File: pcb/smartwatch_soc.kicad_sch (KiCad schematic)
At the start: 39 parts, among them J1 Battery Socket, J2 USB_A, Q1 PN2222A, Q2 PN2222A, Q3 PN2222A, SW1 EN_Switch, SW2 Button, SW3 Button, SW4 Button, SW5 Button, U1 ESP32-S3-MINI-1U, U2 LSM6DS3, U3 OLED_Display, U5 CP2102N-Axx-xQFN20

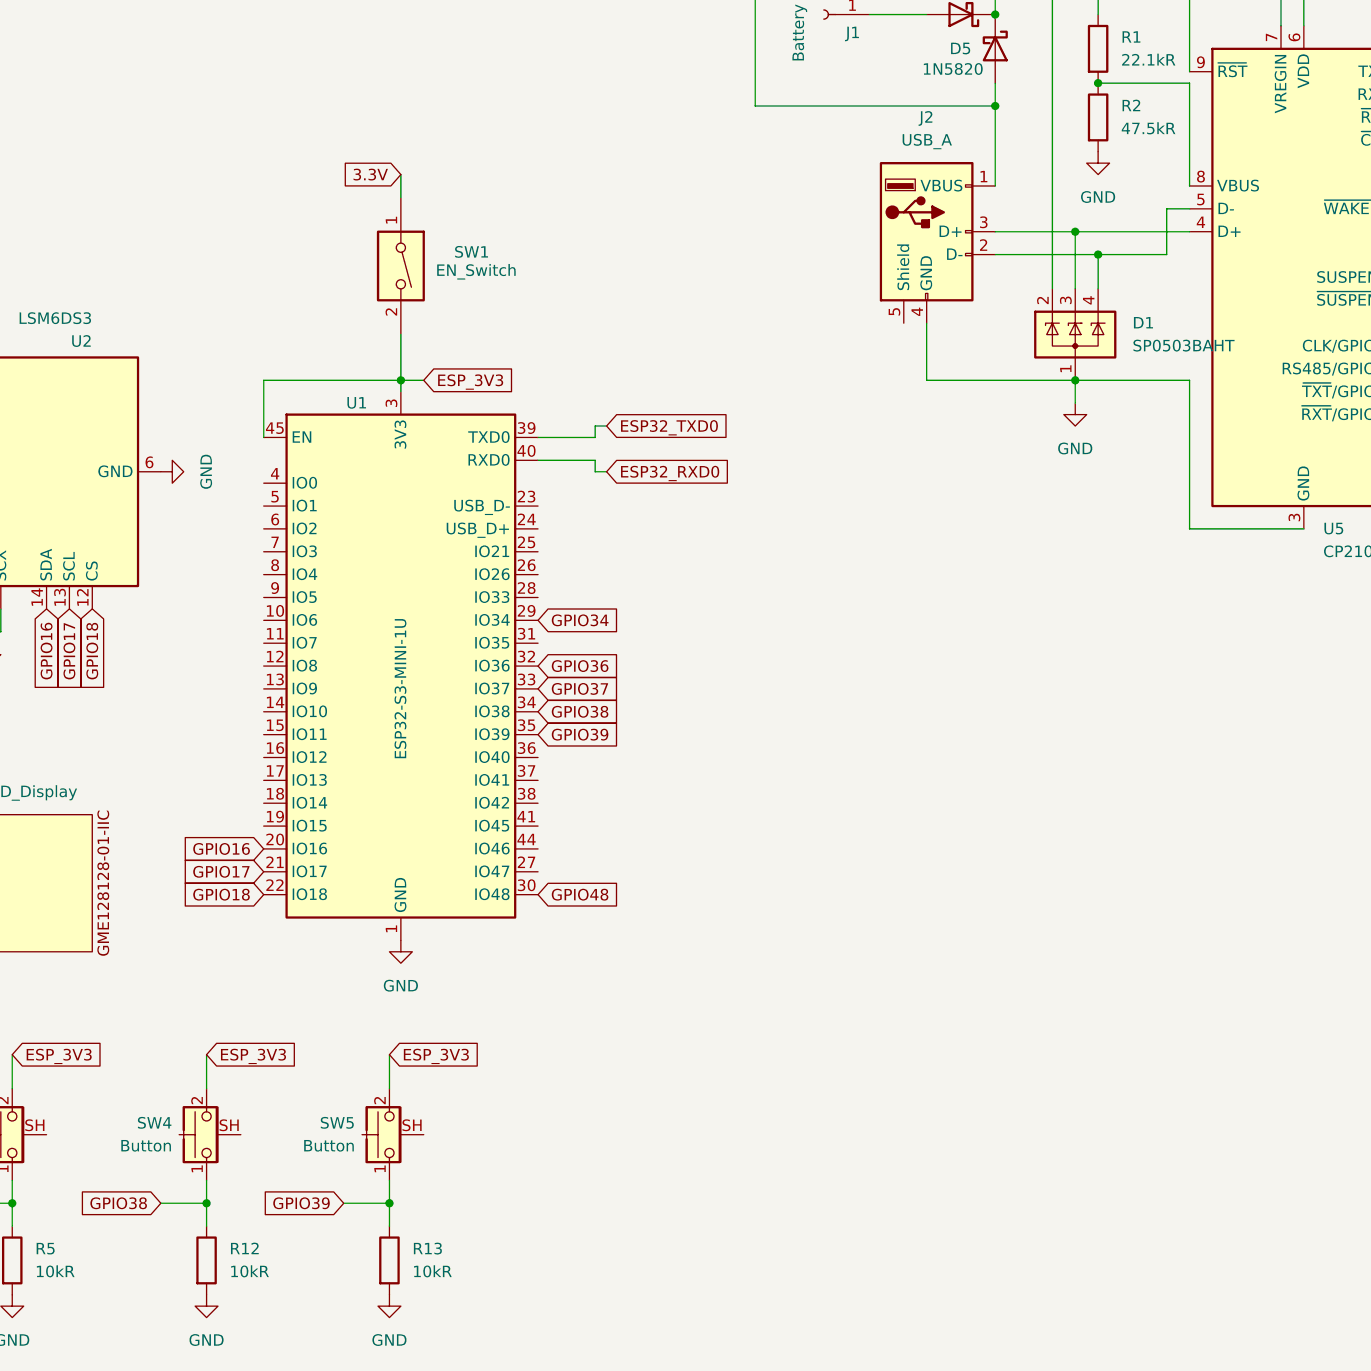
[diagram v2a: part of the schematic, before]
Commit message: added capacitors for en/3.3V for ESP32
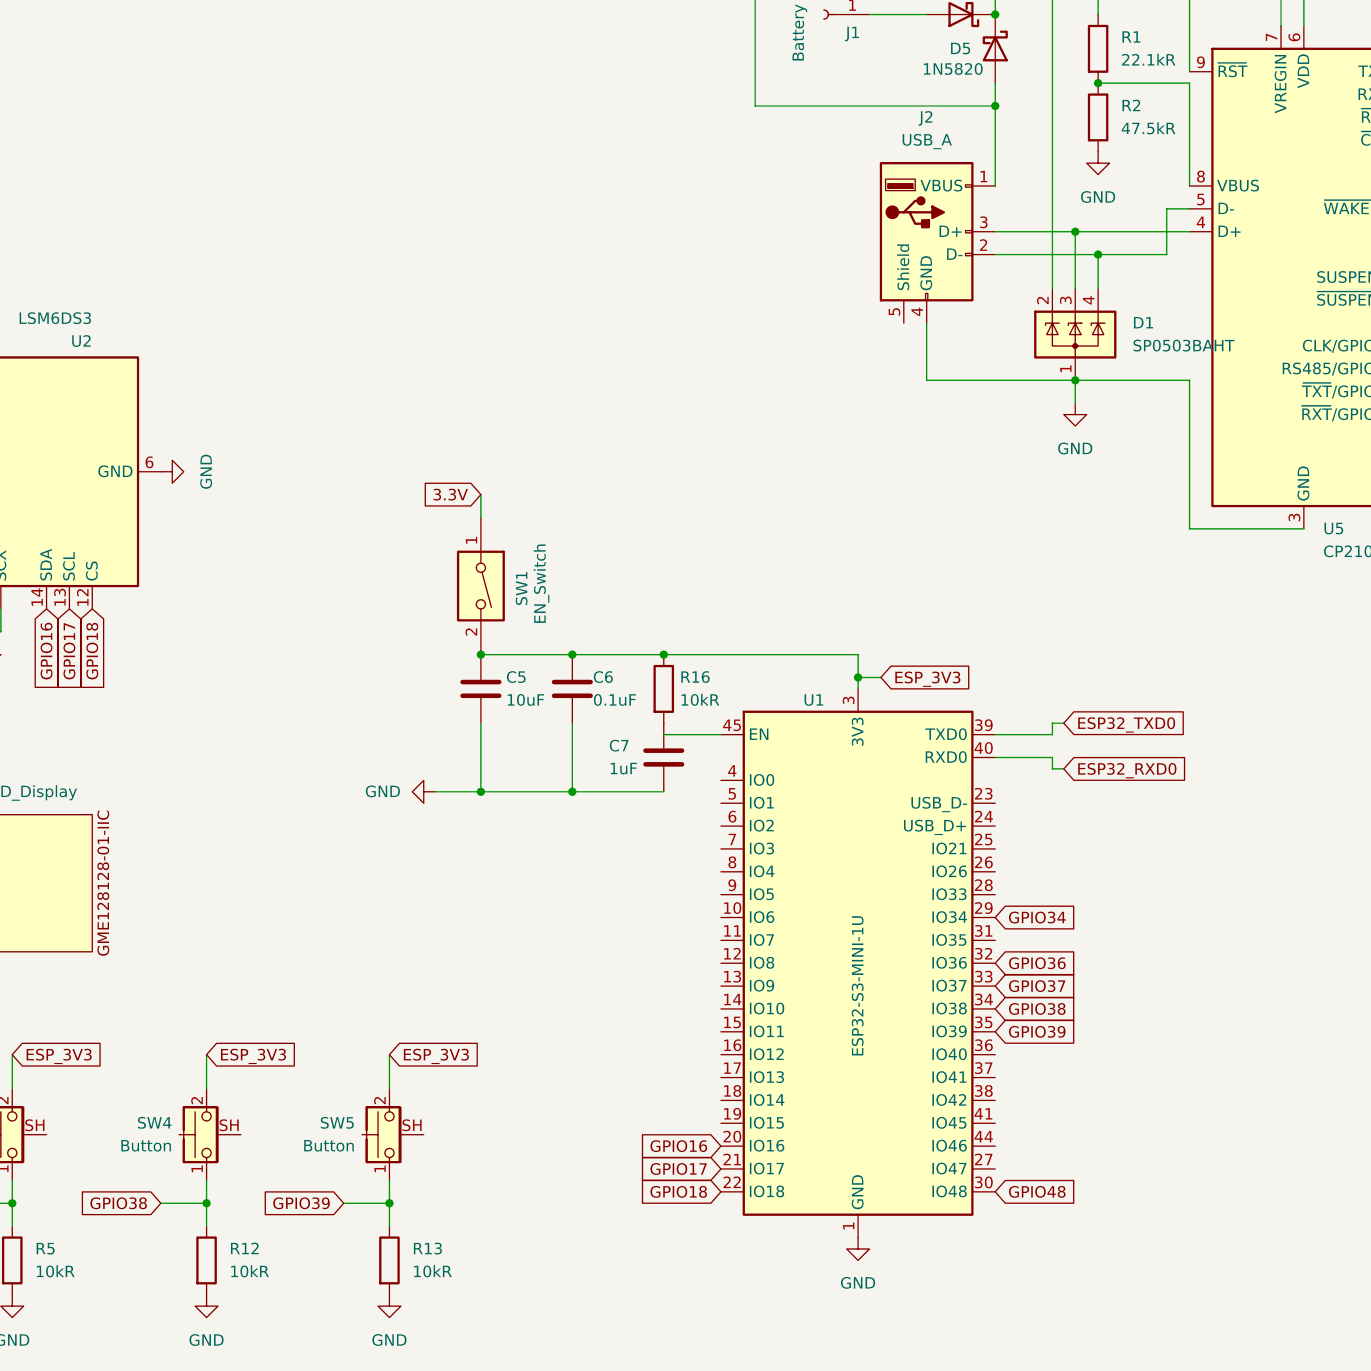
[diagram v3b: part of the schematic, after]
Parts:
- added C5: 10uF, symbol Device:C
- added C6: 0.1uF, symbol Device:C
- added C7: 1uF, symbol Device:C
- added R16: 10kR, symbol Device:R
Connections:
- net ESP_3V3: now also C5.1, C6.1, R16.1; no longer U1.45 (EN)
- net GND: now also C5.2, C6.2, C7.2
- new net: C7.1, R16.2
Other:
- moved on the sheet: SW1, U1

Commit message: bigger schematic page
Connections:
- net ESP32_GPIO0: now reaches U1.4 (IO0)
- net ESP_3V3 renamed ESP32_3V3
- net GPIO16 renamed ESP32_GPIO16
- net GPIO17 renamed ESP32_GPIO17
- net GPIO18 renamed ESP32_GPIO18
- net GPIO34 renamed ESP32_GPIO34
- net GPIO36 renamed ESP32_GPIO36
- net GPIO37 renamed ESP32_GPIO37
- net GPIO38 renamed ESP32_GPIO38
- net GPIO39 renamed ESP32_GPIO39
- net GPIO48 renamed ESP32_GPIO48
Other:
- moved on the sheet: C1, C2, C3, C4, C5, C6, C7, D1, D2, D3, D4, D5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

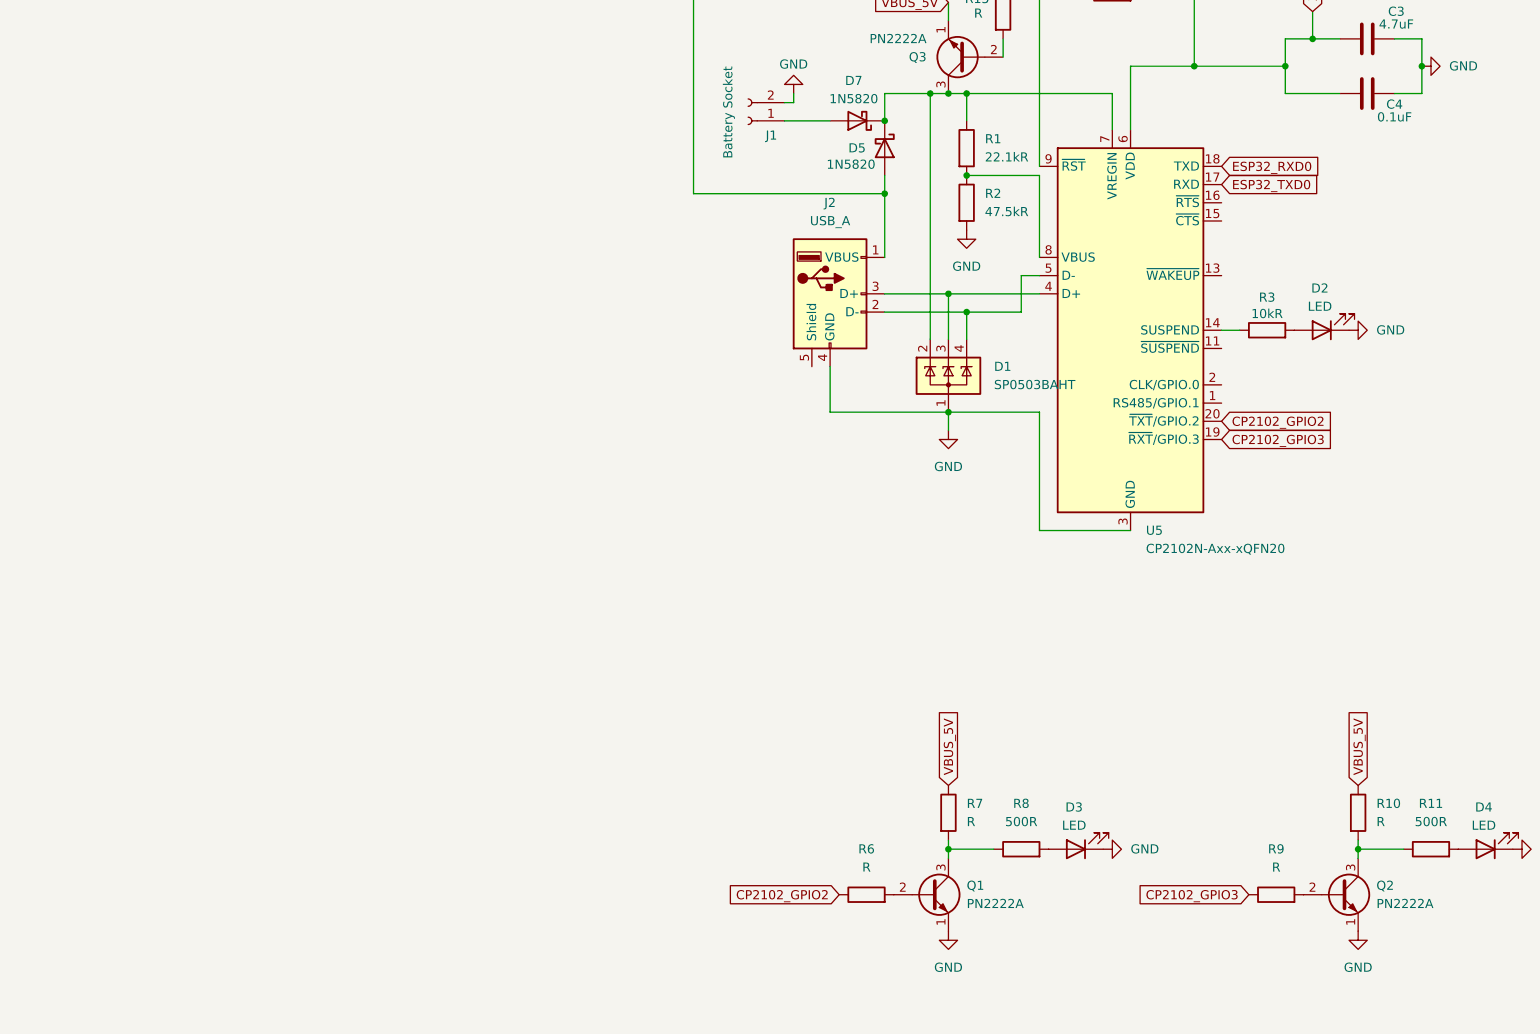
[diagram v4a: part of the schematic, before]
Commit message: switched usba to micro usb type b
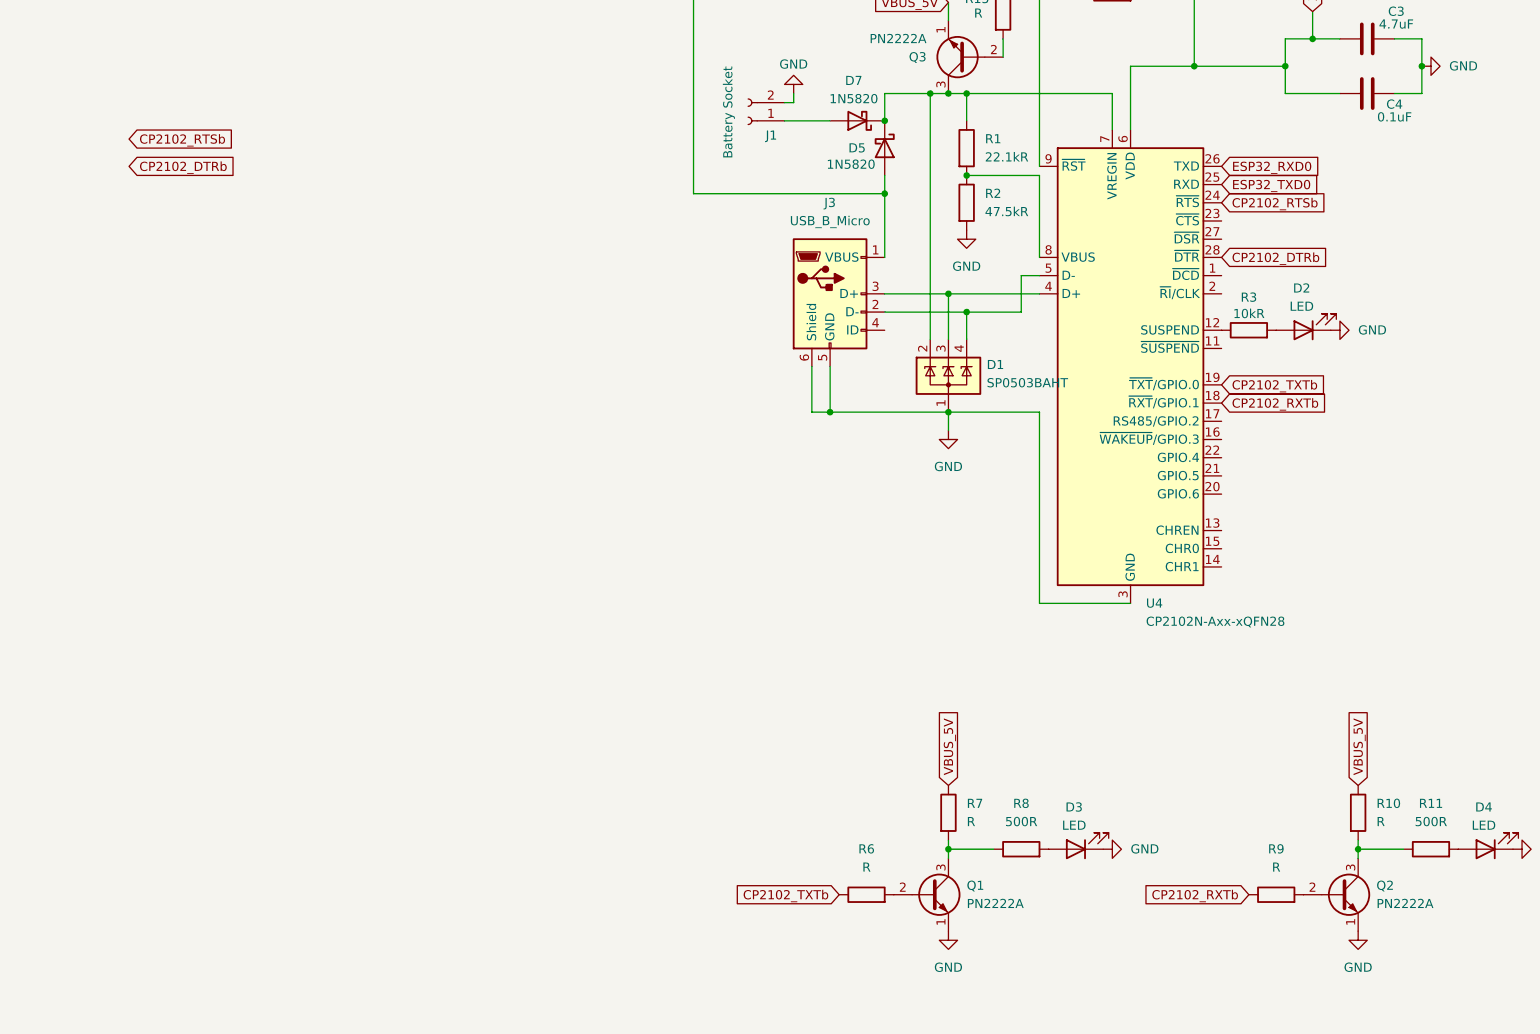
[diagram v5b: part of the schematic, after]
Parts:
- removed J2: USB_A, Connector_USB:USB_A_TE_292303-7_Horizontal, symbol Connector:USB_A
- removed U5: CP2102N-Axx-xQFN20, Package_DFN_QFN:SiliconLabs_QFN-20-1EP_3x3mm_P0.5mm_EP1.8x1.8mm, symbol Interface_USB:CP2102N-Axx-xQFN20
- added J3: USB_B_Micro, symbol Connector:USB_B_Micro
- added U4: CP2102N-Axx-xQFN28, Package_DFN_QFN:QFN-28-1EP_5x5mm_P0.5mm_EP3.35x3.35mm, symbol Interface_USB:CP2102N-Axx-xQFN28
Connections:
- net 3.3V: now also U4.6 (VDD)
- net ESP32_RXD0: now also U4.26 (TXD)
- net ESP32_TXD0: now also U4.25 (RXD)
- net GND: now also J3.5 (GND), J3.6 (Shield), U4.29 (GND), U4.3 (GND)
- net at D5.2 (A), R15.1: now also J3.1 (VBUS)
- net at D1.4 (K): now also J3.2 (D-), U4.5 (D-)
- net at D1.3 (K): now also J3.3 (D+), U4.4 (D+)
- net at R3.1: now also U4.12 (SUSPEND)
- net at D1.2 (K), D5.1 (K), D7.1 (K)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: now also U4.7 (VREGIN)
- net at R1.2, R2.1: now also U4.8 (VBUS)
- net at R14.1: now also U4.9 (~{RST})
- net CP2102_GPIO2 renamed CP2102_TXTb
- net CP2102_TXTb: now also U4.19 (~{TXT}/GPIO.0)
- net CP2102_GPIO3 renamed CP2102_RXTb
- net CP2102_RXTb: now also U4.18 (~{RXT}/GPIO.1)
- new net CP2102_DTRb: U4.28 (~{DTR})
- new net CP2102_RTSb: U4.24 (~{RTS})
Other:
- moved on the sheet: D2, R3

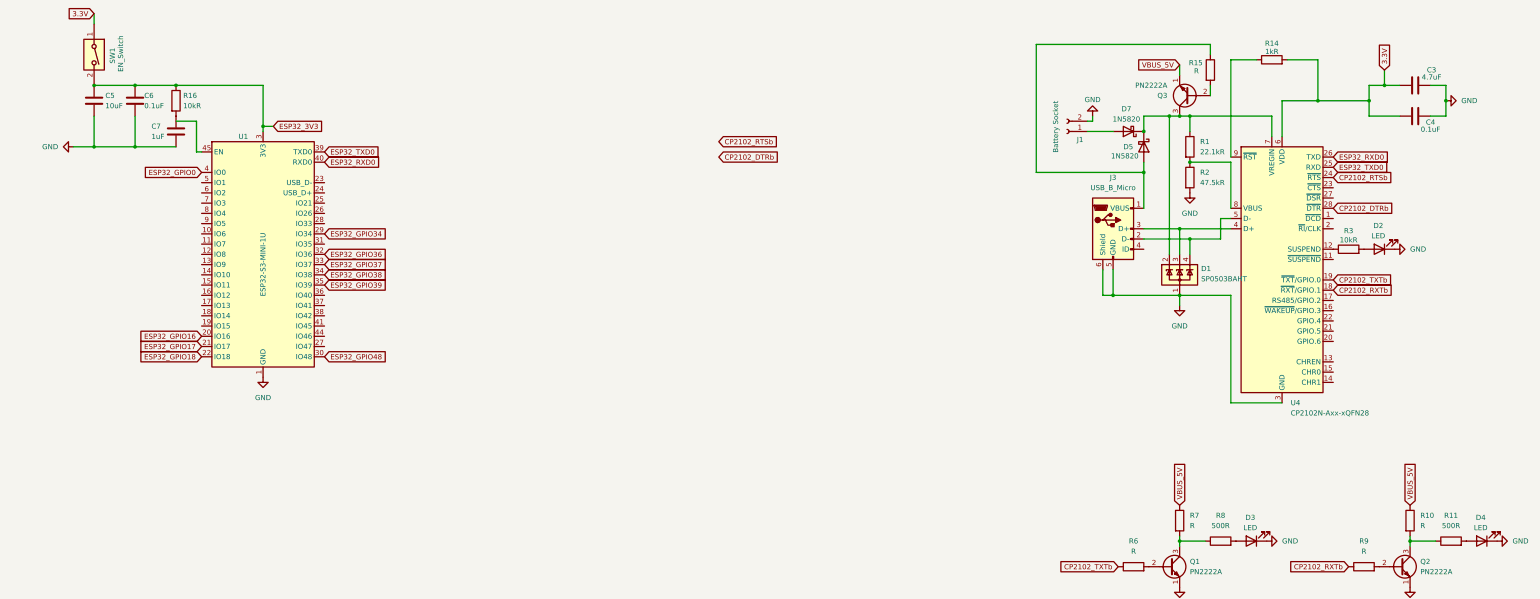
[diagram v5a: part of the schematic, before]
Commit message: referenced esp32-mini devkit
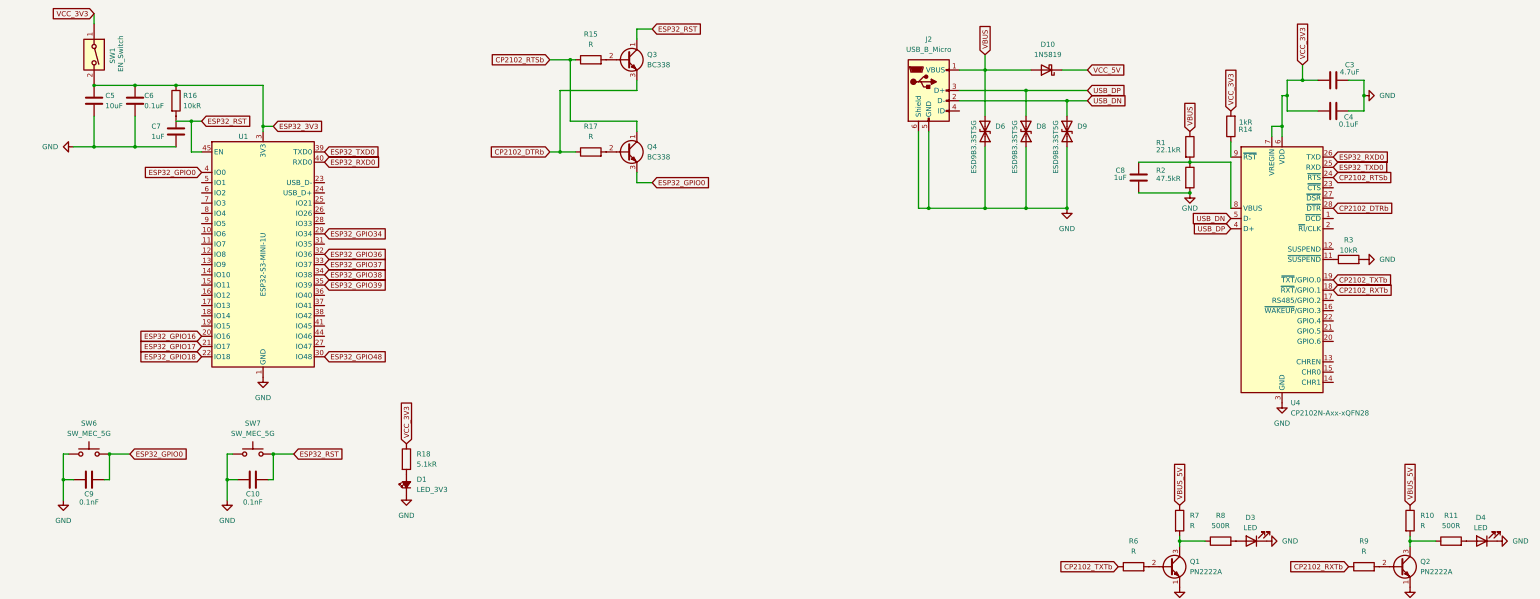
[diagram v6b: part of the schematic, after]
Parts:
- removed D1: SP0503BAHT, Package_TO_SOT_SMD:SOT-143, symbol Power_Protection:SP0503BAHT
- removed D2: LED, LED_THT:LED_D2.0mm_W4.0mm_H2.8mm_FlatTop, symbol Device:LED
- removed D5, D7: 1N5820, Diode_THT:D_DO-201AD_P15.24mm_Horizontal, symbol Diode:1N5820
- removed J1: Battery Socket, Connector_JST:JST_PH_B2B-PH-K_1x02_P2.00mm_Vertical, symbol Connector:Conn_01x02_Socket
- removed J3: USB_B_Micro, symbol Connector:USB_B_Micro
- removed Q3: PN2222A, Package_TO_SOT_THT:TO-92_Inline, symbol Transistor_BJT:PN2222A
- added C10, C9: 0.1nF, symbol Device:C
- added C8: 1uF, Capacitor_THT:C_Disc_D3.0mm_W1.6mm_P2.50mm, symbol Device:C
- added D1: LED_3V3, symbol Device:LED_Small_Filled
- added D10: 1N5819, Diode_THT:D_DO-41_SOD81_P10.16mm_Horizontal, symbol Diode:1N5819
- added D6, D8, D9: ESD9B3.3ST5G, Diode_SMD:D_SOD-923, symbol Diode:ESD9B3.3ST5G
- added J2: USB_B_Micro, symbol Connector:USB_B_Micro
- added Q3, Q4: BC338, Package_TO_SOT_THT:TO-92_Inline, symbol Transistor_BJT:BC338
- added R17: R, symbol Device:R
- added R18: 5.1kR, symbol Device:R
- added SW6, SW7: SW_MEC_5G, symbol Switch:SW_MEC_5G
- R14, R15, R3: footprint Resistor_THT:R_Axial_DIN0204_L3.6mm_D1.6mm_P2.54mm_Vertical -> (none)
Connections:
- net CP2102_DTRb: now also Q3.3 (E), R17.1
- net CP2102_RTSb: now also R15.1, Q4.1 (C)
- net ESP32_GPIO0: now also C9.2, Q4.3 (E), SW6.3 (B), SW6.4 (B)
- net GND: now also R3.2, C10.1, C8.1, C9.1, D1.1 (K), D6.1 (A1), D8.1 (A1), D9.1 (A1), J2.5 (GND), J2.6 (Shield), SW6.1 (A), SW6.2 (A), SW7.1 (A), SW7.2 (A)
- net at U4.11 (~{SUSPEND}): now also R3.1
- net at U4.12 (SUSPEND): no longer R3.1
- net USB_DP: now reaches U4.4 (D+)
- net USB_DP: now also D8.2 (A2), J2.3 (D+)
- net USB_DN: now reaches U4.5 (D-)
- net USB_DN: now also D9.2 (A2), J2.2 (D-)
- net VBUS: now reaches R1.1
- net VBUS: now also D10.2 (A), D6.2 (A2), J2.1 (VBUS); no longer U4.7 (VREGIN)
- net at R1.2, R2.1, U4.8 (VBUS): now also C8.2
- net at R15.2: now also Q3.2 (B)
- net ESP32_RST: now reaches U1.45 (EN)
- net ESP32_RST: now also C10.2, Q3.1 (C), SW7.3 (B), SW7.4 (B)
- net 3.3V renamed VCC_3V3
- net VCC_3V3: now also U4.7 (VREGIN), R18.1
- new net: Q4.2 (B), R17.2
- new net: D1.2 (A), R18.2
- new net VCC_5V: D10.1 (K)
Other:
- moved on the sheet: C3, C4
